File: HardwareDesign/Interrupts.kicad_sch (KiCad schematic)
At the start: 21 parts, among them U401 74HCT74, U402 74HCT11, U403 74HCT147, U404 74HCT540, U405 74HCT574, U406 74HCT32, U407 74HCT32

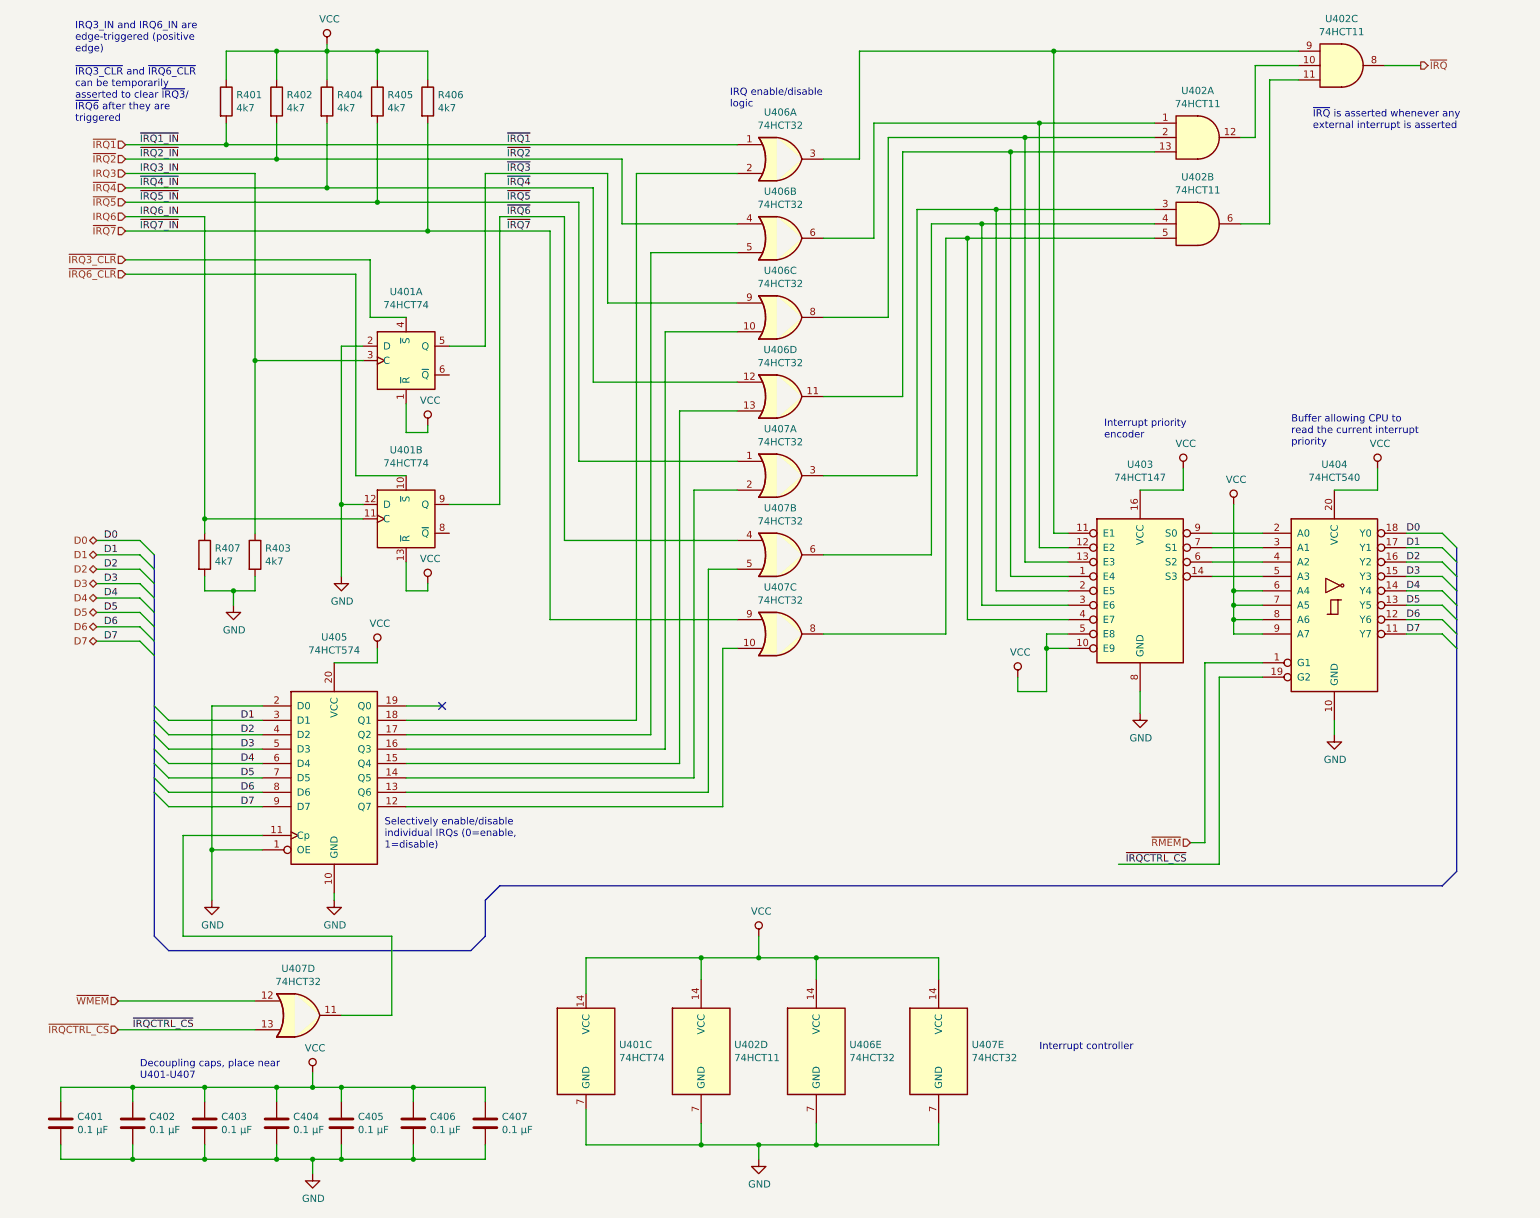
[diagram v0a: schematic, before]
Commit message: initial schematic for FPGA display controller
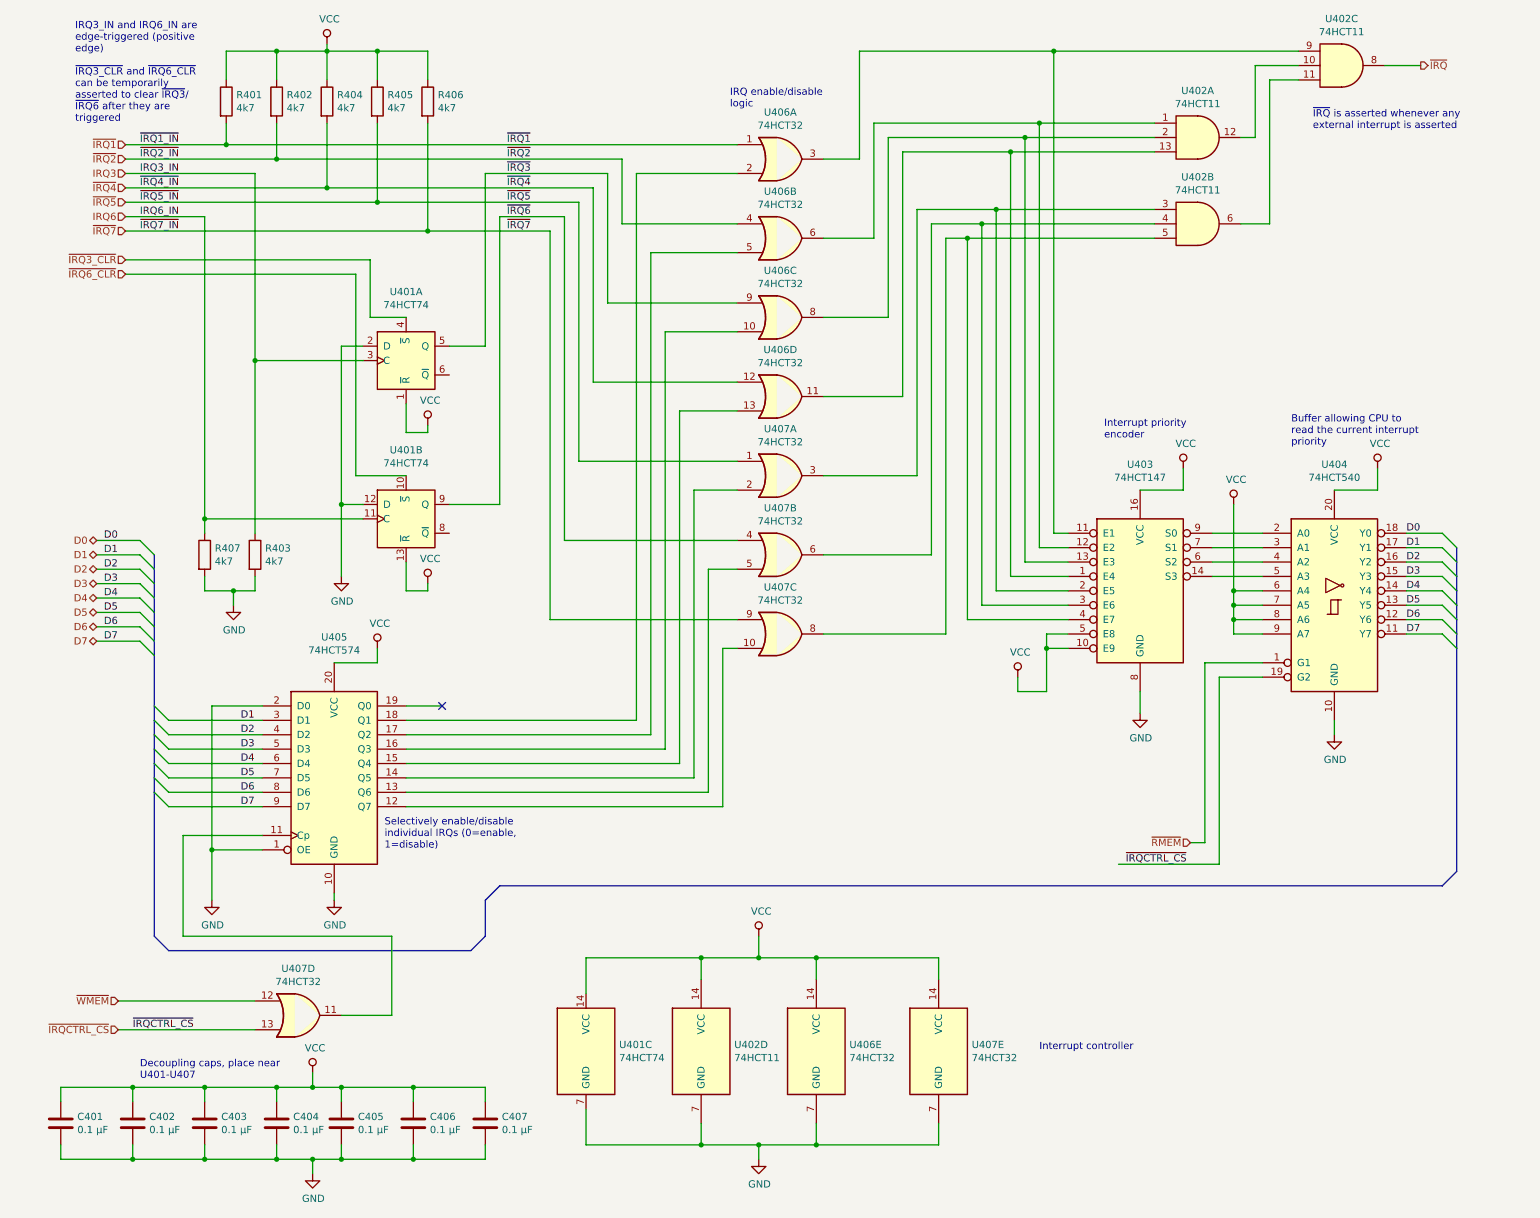
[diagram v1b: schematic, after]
